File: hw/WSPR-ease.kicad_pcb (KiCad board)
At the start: 4 copper layers, 99 x 64 mm, 123 parts, among them J101 SMA, J102 SMA, J103 640-USB4930-00-A, Q101 MMBF170, Q301 MMBF170, Q302 MMBF170, Q303 MMBF170, Q304 MMBF170, Q305 MMBF170, Q306 MMBF170, Q307 MMBF170, Q308 MMBF170, Q309 MMBF170, Q310 MMBF170, Q311 MMBF170, Q312 MMBF170, T301 BN-43-202_DualPri_CTSec, U101 GNSS module, U102 ESP32-S3-WROOM-1-N8R8, U103 TPS22918DBVR, U104 TPS74612PQWDRBRQ1, U105 SRV05-4, U106 LMR51430YDDCR, U201 AS183-92LF, U202 AS183-92LF, U203 AS183-92LF, U204 AS183-92LF, U301 ICE40UP5K-SG48ITR, U302 CD74ACT541SM96, Y301 40MHz

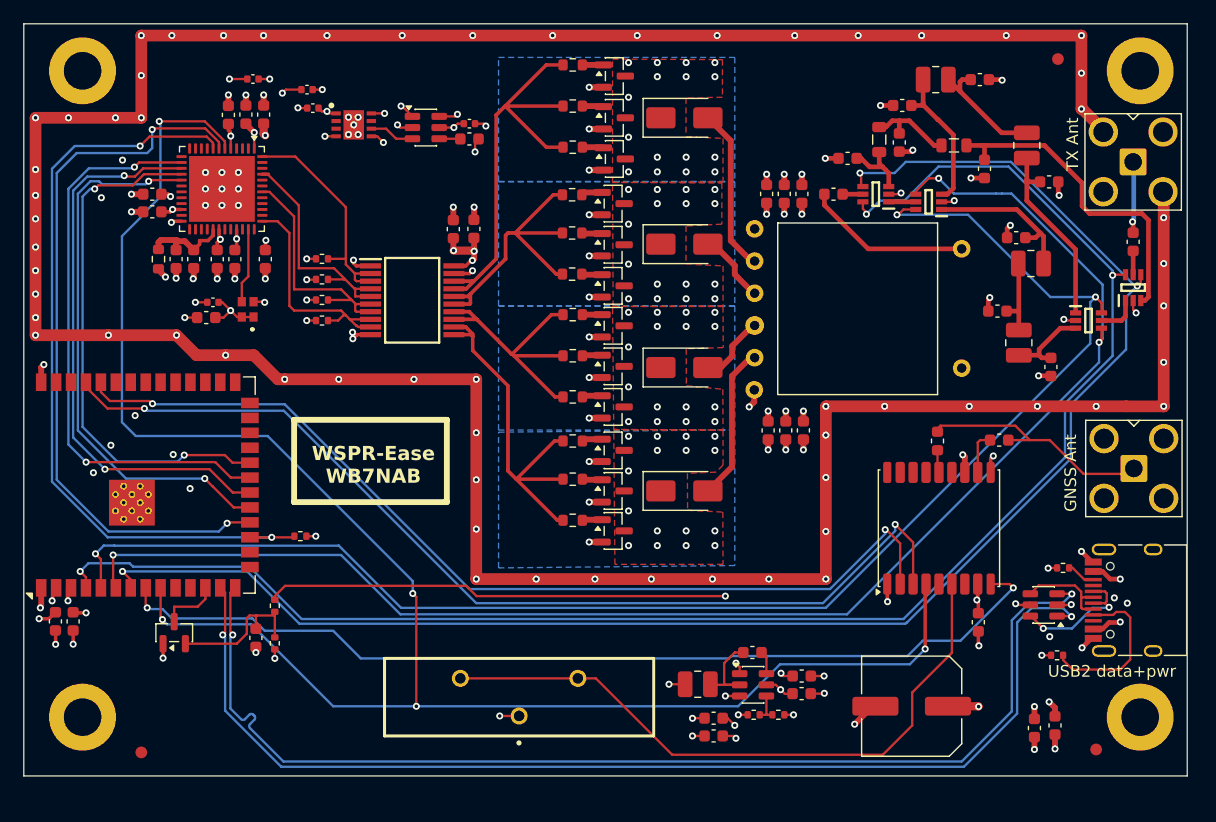
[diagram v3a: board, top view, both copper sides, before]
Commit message: About to redo the layout of the tx gate controls to match lengths
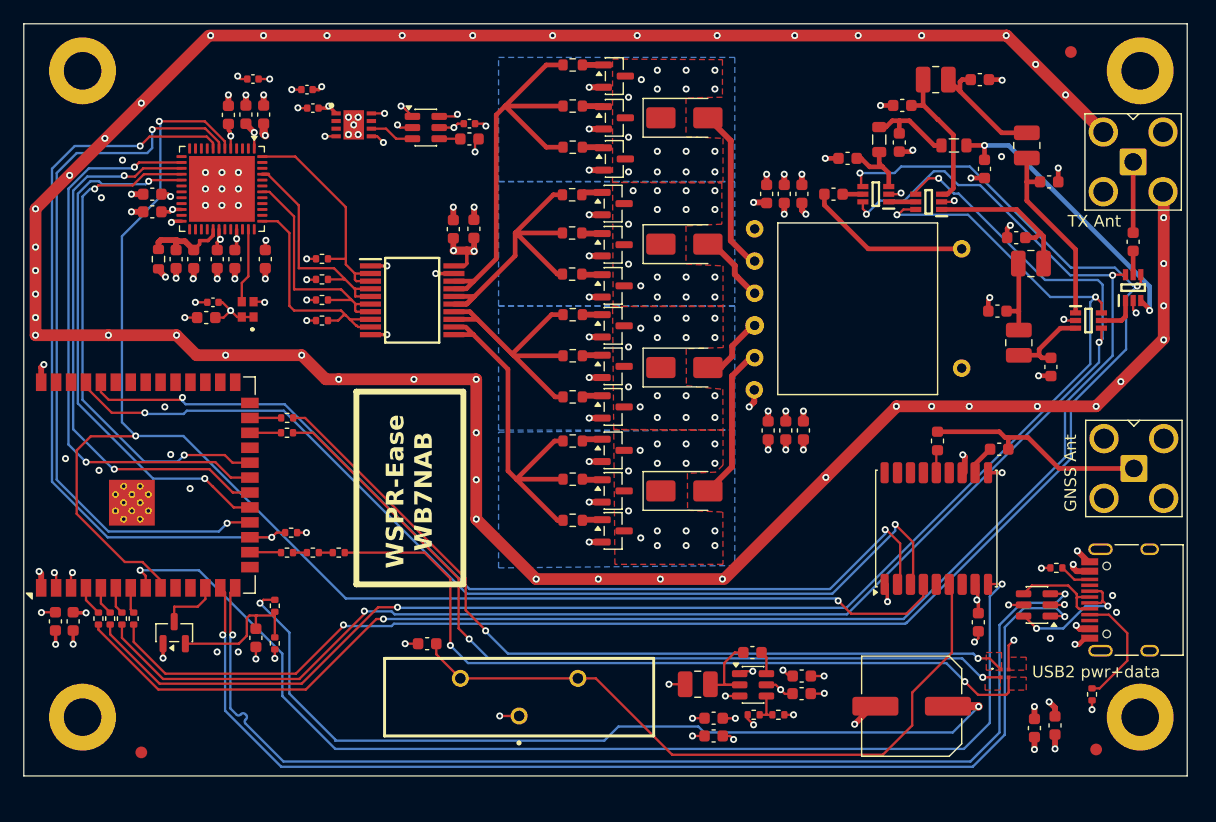
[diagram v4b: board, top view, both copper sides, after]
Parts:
- removed J103: 640-USB4930-00-A, Library:USB_C_Receptacle_HRO_TYPE-C-31-M-12-bursted
- added C117: 10uF X5R 25V, Capacitor_SMD:C_0603_1608Metric, F.Cu at (83.9, 122.2)
- added D101: LED_BGRA, Library:UHD111AFKAC3K23E1L3VG5ZB3Z3, F.Cu at (133.1, 124.7)
- added J1301: pwr+data, Library:USB_C_Receptacle_HRO_TYPE-C-31-M-12-bursted, F.Cu at (144.3, 118.4)
- added R107: 22, Resistor_SMD:R_0402_1005Metric, F.Cu at (56.0, 120.0)
- added R108: 22, Resistor_SMD:R_0402_1005Metric, F.Cu at (57.0, 120.0)
- added R109: 22, Resistor_SMD:R_0402_1005Metric, F.Cu at (58.0, 120.0)
- added R110: 22, Resistor_SMD:R_0402_1005Metric, F.Cu at (59.0, 120.0)
- added R111: 100, Resistor_SMD:R_0402_1005Metric, F.Cu at (74.2, 114.4)
- added R112: 100, Resistor_SMD:R_0402_1005Metric, F.Cu at (72.0, 104.2)
- added R113: 100, Resistor_SMD:R_0402_1005Metric, F.Cu at (72.0, 102.9)
- added R114: 100, Resistor_SMD:R_0402_1005Metric, F.Cu at (76.4, 114.4)
- added R120: 100, Resistor_SMD:R_0402_1005Metric, F.Cu at (72.0, 114.4)
- moved R103 4.46 mm to (140.5, 126.5), turned to -90 degrees
- moved FID102 1.25 mm to (138.7, 71.8)
- moved R301 0.84 mm to (72.3, 112.7)
- moved C103 0.77 mm to (132.6, 105.6)
- moved R104 0.57 mm to (137.5, 115.7)
- moved U105 0.57 mm to (135.8, 118.8)
- moved U101 0.23 mm to (127.2, 112.3)
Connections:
- U102 pad 13: /D+ -> /D-
- U102 pad 14: /D- -> /D+
- U102 pad 16: unconnected-(U102-IO46-Pad16) -> Net-(U102-IO46)
- U102 pad 24: unconnected-(U102-IO47-Pad24) -> Net-(U102-IO47)
- U102 pad 25: unconnected-(U102-IO48-Pad25) -> Net-(U102-IO48)
- U102 pad 4: /loON -> Net-(U102-IO4)
- U102 pad 5: /lo1ON -> Net-(U102-IO5)
- U102 pad 6: /lo2ON -> Net-(U102-IO6)
- U102 pad 7: /hiON -> Net-(U102-IO7)
- U105 pad 1: /D+ -> /D-
- U105 pad 3: /D- -> /D+
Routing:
- net /grn: track 0.00 -> 71.2 mm, vias 0 -> 2
- net /blu: track 0.00 -> 70.7 mm, vias 0 -> 2
- net /red: track 0.00 -> 66.2 mm, vias 0 -> 2
- net VBUS: track 61.3 -> 92.2 mm
- net GND: track 367.5 -> 337.4 mm, vias 171 -> 162
- net /gnssPPS: track 153.2 -> 131.6 mm, vias 5 -> 3
- net /gnssNRESET: track 81.8 -> 96.5 mm
- net /Transmitter/push1G: track 24.1 -> 35.7 mm
- net +3.3V: track 19.4 -> 23.7 mm, vias 15 -> 16
- net Net-(U101-V_BCKP): track 55.6 -> 59.4 mm
- net Net-(J1301-CC1): track 13.8 -> 10.2 mm
- net Net-(U204-J3): track 27.8 -> 25.0 mm, vias 0 -> 2
- net Net-(U102-IO48): track 0.00 -> 2.66 mm
- net Net-(U102-IO47): track 0.00 -> 2.64 mm
- net Net-(U102-IO46): track 0.00 -> 2.61 mm
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- added copper zone on F.Cu, net +3.3V
- added copper zone on F.Cu, net /blu
- added copper zone on F.Cu, net /grn
- added copper zone on F.Cu, net /red

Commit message: Fix huge oopsie with USB diode protection after having fixed the unforgivable polarity reversal and NOT SEEING THIS BUG. I can be an idiot sometimes.
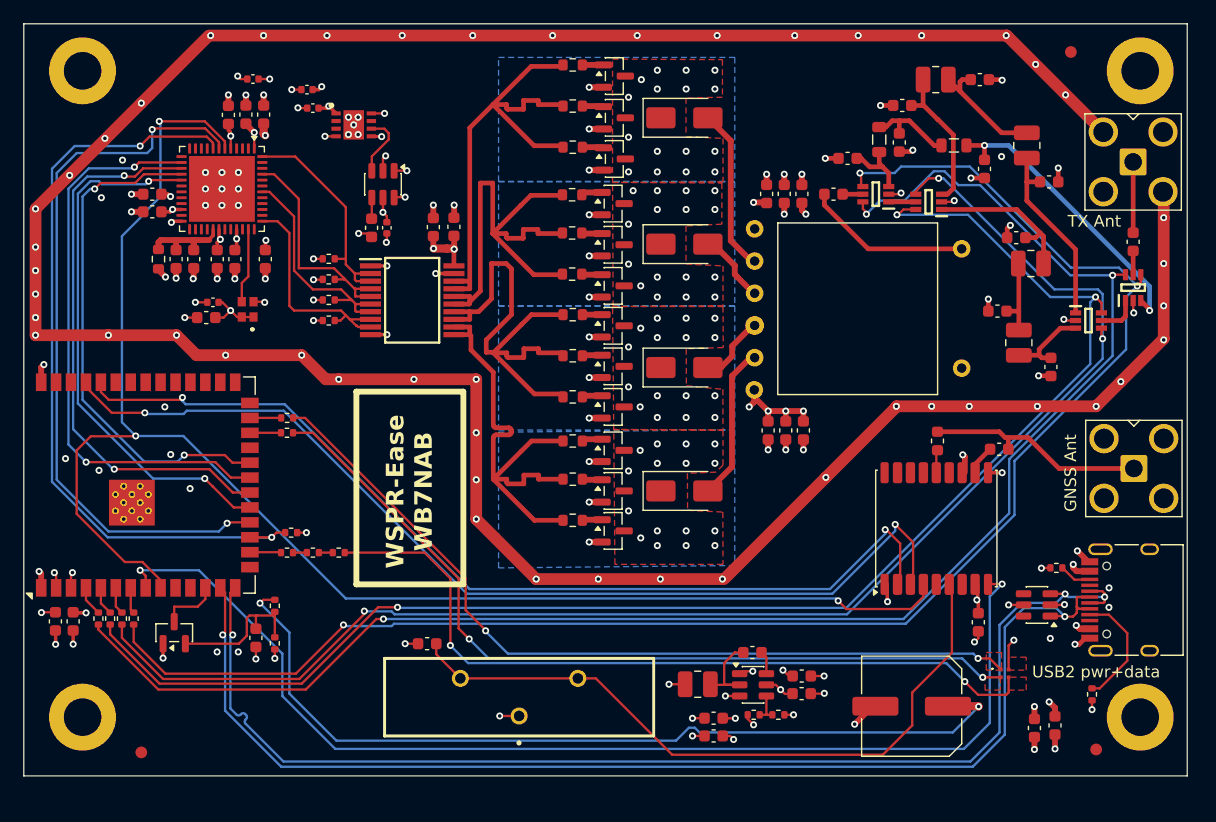
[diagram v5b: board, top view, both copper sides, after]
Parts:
- moved C108 11.3 mm to (80.5, 86.8), turned to -90 degrees
- moved C106 11.2 mm to (79.2, 86.8), turned to -90 degrees
- moved U103 6.04 mm to (80.2, 83.0), turned to -90 degrees
- moved C308 1.71 mm to (84.5, 86.7)
- moved C309 1.71 mm to (86.2, 86.7)
- moved R302 0.58 mm to (75.5, 91.2)
- moved R303 0.58 mm to (75.5, 89.4)
- moved R304 0.58 mm to (75.5, 92.9)
- moved R305 0.58 mm to (75.5, 94.7)
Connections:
- J1301 pad A6: Net-(U105-IO4) -> /D+
- J1301 pad A7: Net-(U105-IO3) -> /D-
- J1301 pad B6: Net-(U105-IO4) -> /D+
- J1301 pad B7: Net-(U105-IO3) -> /D-
- U105 pad 4: Net-(U105-IO3) -> unconnected-(U105-IO3-Pad4)
- U105 pad 6: Net-(U105-IO4) -> unconnected-(U105-IO4-Pad6)
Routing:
- net /Transmitter/pull1G: track 27.4 -> 41.2 mm
- net Net-(U105-IO4): track 12.0 -> 0.00 mm, vias 2 -> 0
- net Net-(U105-IO3): track 8.50 -> 0.00 mm
- net /D+: track 96.7 -> 103.5 mm, vias 2 -> 3
- net /Transmitter/push2G: track 34.4 -> 41.2 mm
- net /Transmitter/push1G: track 35.7 -> 41.2 mm
- net VBUS: track 92.2 -> 97.3 mm
- net /D-: track 96.7 -> 101.5 mm
- net /Transmitter/pull2G: track 37.3 -> 41.3 mm
- net +VFPGAIO: track 24.4 -> 22.5 mm
- net Net-(U103-ON): track 3.85 -> 5.44 mm
- net /Transmitter/push1: track 20.6 -> 19.2 mm
- net /lo2ON: track 125.6 -> 124.8 mm
- net /Transmitter/pull1: track 20.2 -> 19.5 mm
- net +3.3V: track 23.7 -> 23.1 mm

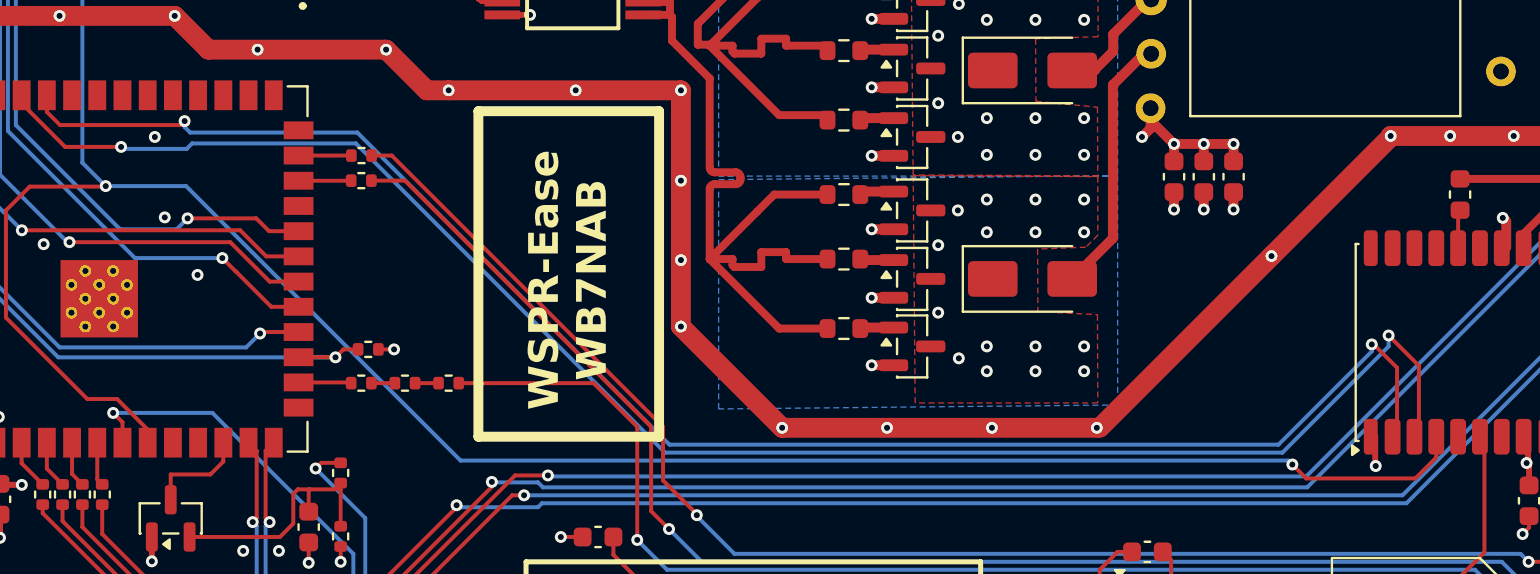
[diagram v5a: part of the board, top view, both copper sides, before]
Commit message: Oops. Rx and Tx need to be swapped on GNSS
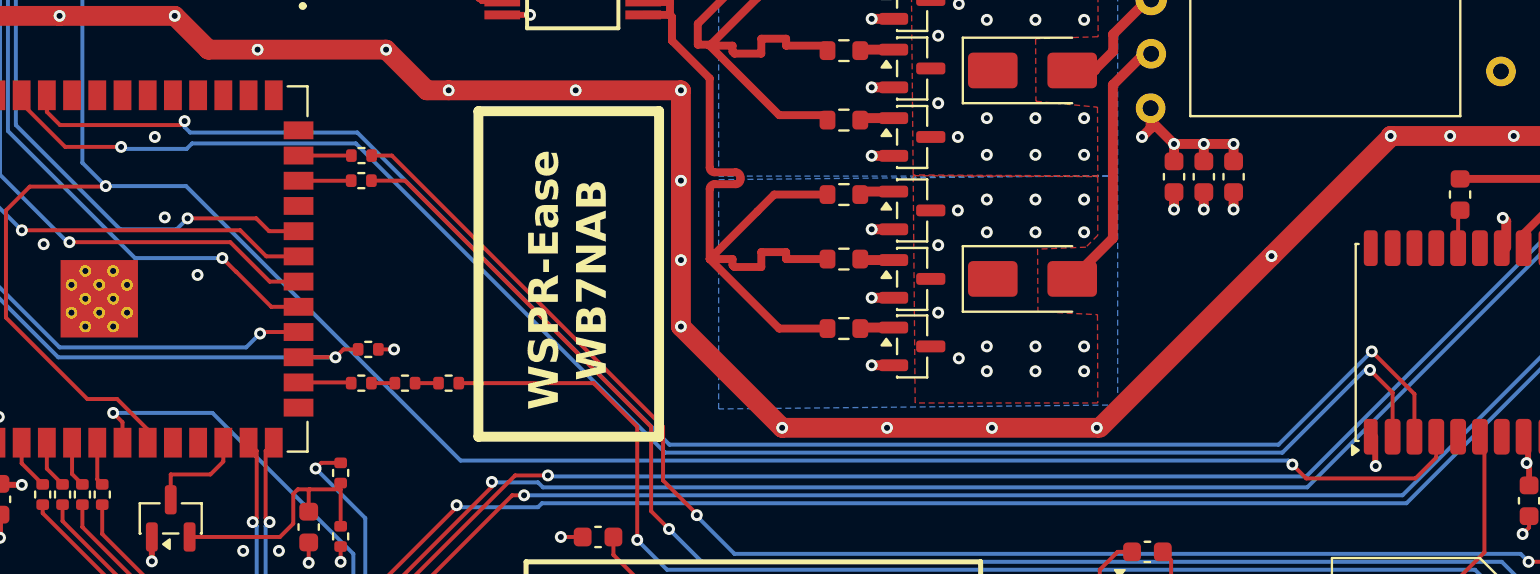
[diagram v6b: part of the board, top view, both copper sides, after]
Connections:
- U101 pad 2: /gnssTx -> /gnssRx
- U101 pad 3: /gnssRx -> /gnssTx
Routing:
- net /gnssRx: track 84.8 -> 81.0 mm
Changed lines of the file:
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@@
 			(layers "F.Cu" "F.Mask" "F.Paste")
 			(roundrect_rratio 0.25)
-			(net 9 "/gnssTx")
+			(net 8 "/gnssRx")
 			(pinfunction "TXD")
 			(pintype "output")
@@
 			(layers "F.Cu" "F.Mask" "F.Paste")
 			(roundrect_rratio 0.25)
-			(net 8 "/gnssRx")
+			(net 9 "/gnssTx")
 			(pinfunction "RXD")
 			(pintype "input")
@@
 	)
 	(segment
-		(start 125.275 113.525)
-		(end 123.75 112)
+		(start 123.95 117.1)
+		(end 123.95 114.875)
 		(width 0.2)
 		(layer "F.Cu")
@@
 	)
 	(segment
-		(start 125.275 117.075)
-		(end 125.275 113.525)
+		(start 123.95 114.875)
+		(end 122.811765 113.736765)
 		(width 0.2)
 		(layer "F.Cu")
@@
 	)
 	(via
-		(at 123.75 112)
+		(at 122.811765 113.736765)
 		(size 0.6)
 		(drill 0.3)
@@
 	)
 	(segment
-		(start 123.75 112.55)
-		(end 123.75 112)
+		(start 63.2 102.6)
+		(end 60 102.6)
 		(width 0.2)
 		(layer "B.Cu")
@@
 	(segment
 		(start 87.3 117.9)
-		(end 118.4 117.9)
+		(end 71.725 102.325)
 		(width 0.2)
 		(layer "B.Cu")
@@
 	(segment
 		(start 71.725 102.325)
-		(end 87.3 117.9)
+		(end 63.475 102.325)
 		(width 0.2)
 		(layer "B.Cu")
@@
 	)
 	(segment
-		(start 59.9 102.5)
-		(end 60 102.6)
+		(start 122.811765 113.736765)
+		(end 122.563235 113.736765)
 		(width 0.2)
 		(layer "B.Cu")
@@
 	)
 	(segment
-		(start 60 102.6)
+		(start 63.475 102.325)
 		(end 63.2 102.6)
 		(width 0.2)
@@
 	)
 	(segment
-		(start 63.2 102.6)
-		(end 63.475 102.325)
+		(start 60 102.6)
+		(end 59.9 102.5)
 		(width 0.2)
 		(layer "B.Cu")
@@
 	)
 	(segment
-		(start 118.4 117.9)
-		(end 123.75 112.55)
+		(start 122.563235 113.736765)
+		(end 118.4 117.9)
 		(width 0.2)
 		(layer "B.Cu")
@@
 	)
 	(segment
-		(start 63.475 102.325)
-		(end 71.725 102.325)
+		(start 118.4 117.9)
+		(end 87.3 117.9)
 		(width 0.2)
 		(layer "B.Cu")
@@
 	)
 	(segment
-		(start 122.9 112.45)
-		(end 123 112.45)
+		(start 56.825 101.4)
+		(end 56.16 100.735)
 		(width 0.2)
 		(layer "F.Cu")
@@
 	)
 	(segment
-		(start 123 112.45)
-		(end 124.175 113.625)
+		(start 56.16 100.735)
+		(end 56.16 99.9)
 		(width 0.2)
 		(layer "F.Cu")
@@
 	)
 	(segment
-		(start 56.825 101.4)
-		(end 56.16 100.735)
+		(start 63.1 101.2)
+		(end 62.9 101.4)
 		(width 0.2)
 		(layer "F.Cu")
@@
 	)
 	(segment
-		(start 124.175 113.625)
-		(end 124.175 117.075)
+		(start 62.9 101.4)
+		(end 56.825 101.4)
 		(width 0.2)
 		(layer "F.Cu")
@@
 	)
 	(segment
-		(start 56.16 100.735)
-		(end 56.16 99.9)
+		(start 125.05 117.1)
+		(end 125.05 114.95)
 		(width 0.2)
 		(layer "F.Cu")
@@
 	)
 	(segment
-		(start 63.1 101.2)
-		(end 62.9 101.4)
+		(start 125.05 114.95)
+		(end 122.9 112.8)
 		(width 0.2)
 		(layer "F.Cu")
@@
 	)
 	(segment
-		(start 62.9 101.4)
-		(end 56.825 101.4)
+		(start 122.9 112.8)
+		(end 123 112.7)
 		(width 0.2)
 		(layer "F.Cu")
@@
 	)
 	(via
-		(at 122.9 112.45)
+		(at 122.9 112.8)
 		(size 0.6)
 		(drill 0.3)
@@
 	)
 	(segment
-		(start 71.8 101.775)
-		(end 87.524 117.499)
-		(width 0.2)
-		(layer "B.Cu")
-		(net 9)
-	)
-	(segment
 		(start 63.1 101.5)
-		(end 63.375 101.775)
+		(end 63.1 101.2)
 		(width 0.2)
 		(layer "B.Cu")
@@
 	(segment
 		(start 118.201 117.499)
-		(end 122.9 112.8)
+		(end 87.524 117.499)
 		(width 0.2)
 		(layer "B.Cu")
@@
 	(segment
 		(start 63.375 101.775)
-		(end 71.8 101.775)
+		(end 63.1 101.5)
 		(width 0.2)
 		(layer "B.Cu")
@@
 	(segment
 		(start 122.9 112.8)
-		(end 122.9 112.45)
+		(end 118.201 117.499)
 		(width 0.2)
 		(layer "B.Cu")
@@
 	(segment
 		(start 87.524 117.499)
-		(end 118.201 117.499)
+		(end 71.8 101.775)
 		(width 0.2)
 		(layer "B.Cu")
@@
 	)
 	(segment
-		(start 63.1 101.2)
-		(end 63.1 101.5)
+		(start 71.8 101.775)
+		(end 63.375 101.775)
 		(width 0.2)
 		(layer "B.Cu")

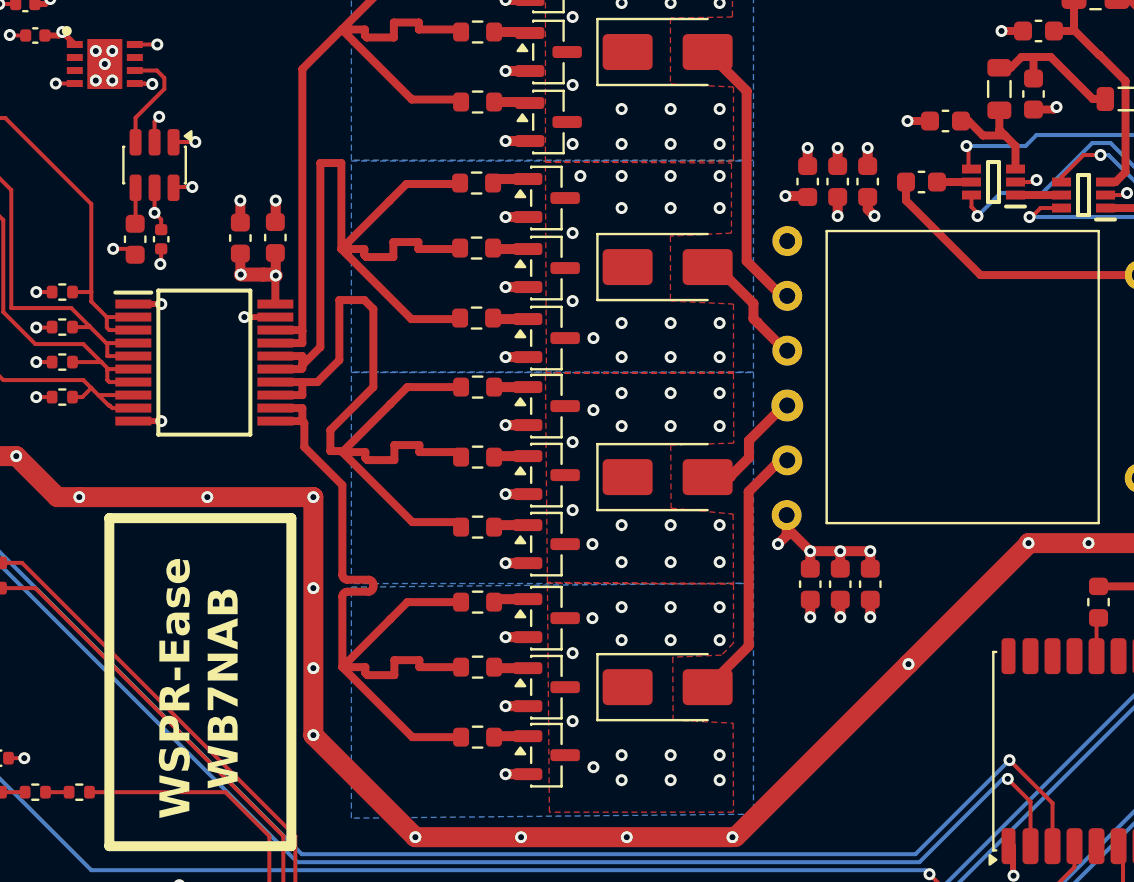
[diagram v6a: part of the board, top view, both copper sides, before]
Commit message: Fixed reversed rx/tx on GNSS chip. Solved all ERC and DRC issues
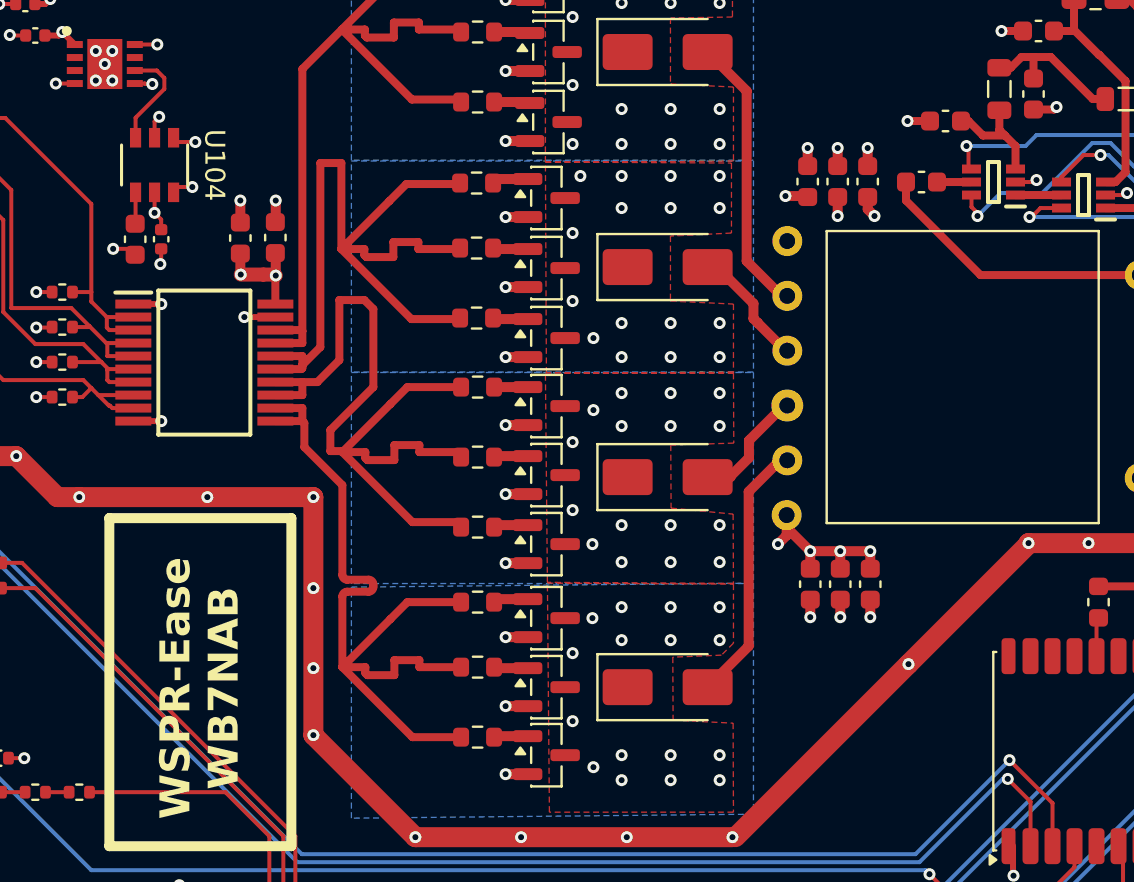
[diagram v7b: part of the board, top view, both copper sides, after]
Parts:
- U104: renamed from U103; footprint Package_TO_SOT_SMD:SOT-23-6 -> Library:DBV6_TEX
- renumbered C102 to C101, C101 to C102, C117 to C103, C103 to C104, C104 to C105, C105 to C106, C106 to C107, C107 to C108, C108 to C109, C113 to C110, C112 to C111, C110 to C112, C109 to C113, C111 to C114, C114 to C115, C115 to C116, C116 to C117, J1301 to J103, R107 to R103, R108 to R104, R109 to R105, R110 to R106, R120 to R107, R111 to R108, R112 to R109, R113 to R110, R114 to R111, R103 to R112, R104 to R113, R105 to R114, R106 to R115, U105 to U103, U104 to U105
